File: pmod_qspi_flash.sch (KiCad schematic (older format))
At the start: 1 part, among them P1 PMOD-Device-x2-Type-Generic-A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

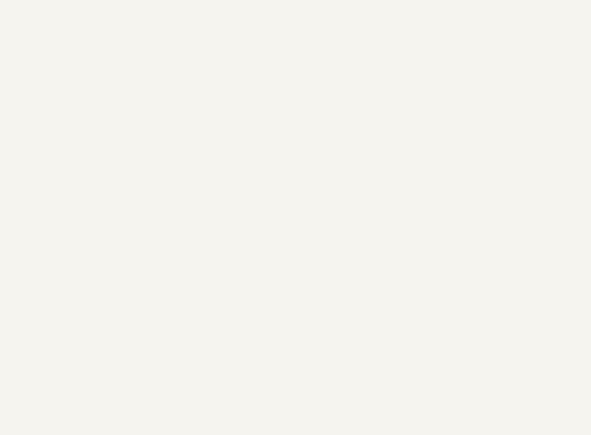
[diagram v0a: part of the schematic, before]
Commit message: add qspi flash symbol and footprint
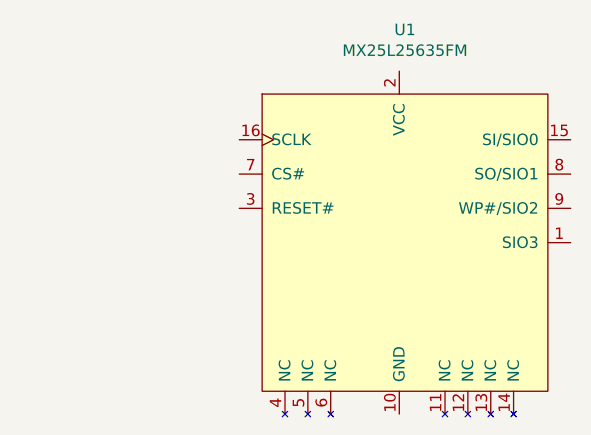
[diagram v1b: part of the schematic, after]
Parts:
- added U1: MX25L25635FM, Package_SO:SOIC-16W_7.5x10.3mm_P1.27mm, symbol qspi_flash:MX25L25635FM
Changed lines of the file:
@@
+	1    0    0    -1
+$EndComp
+$Comp
+L qspi_flash:MX25L25635FM U1
+U 1 1 6135200C
+P 5550 3750
+F 0 "U1" H 5575 4681 50  0000 C CNN
+F 1 "MX25L25635FM" H 5575 4590 50  0000 C CNN
+F 2 "Package_SO:SOIC-16W_7.5x10.3mm_P1.27mm" H 5050 4500 50  0001 C CNN
+F 3 "" H 5050 4500 50  0001 C CNN
+	1    5550 3750
 	1    0    0    -1
 $EndComp

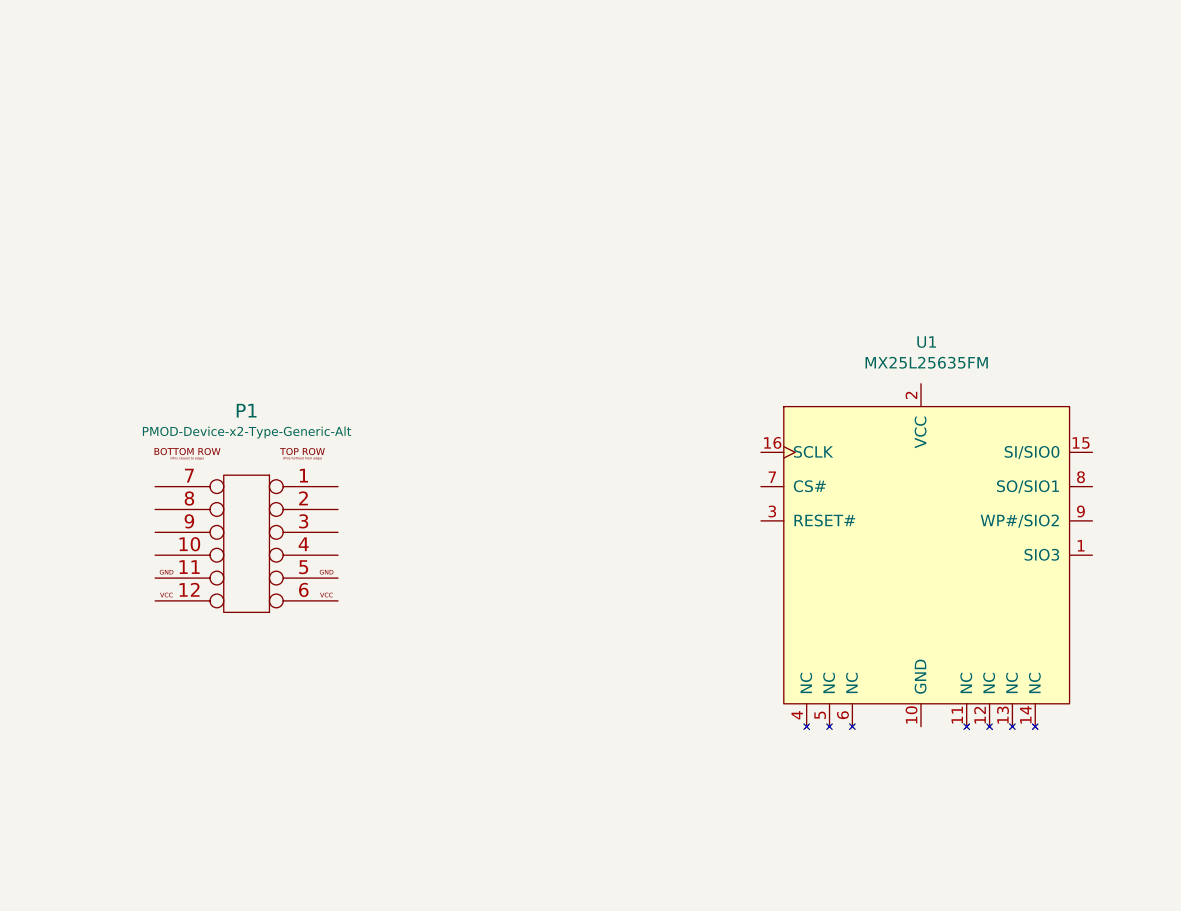
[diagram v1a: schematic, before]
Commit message: routed but ugly, need to rotate flash to align with signals
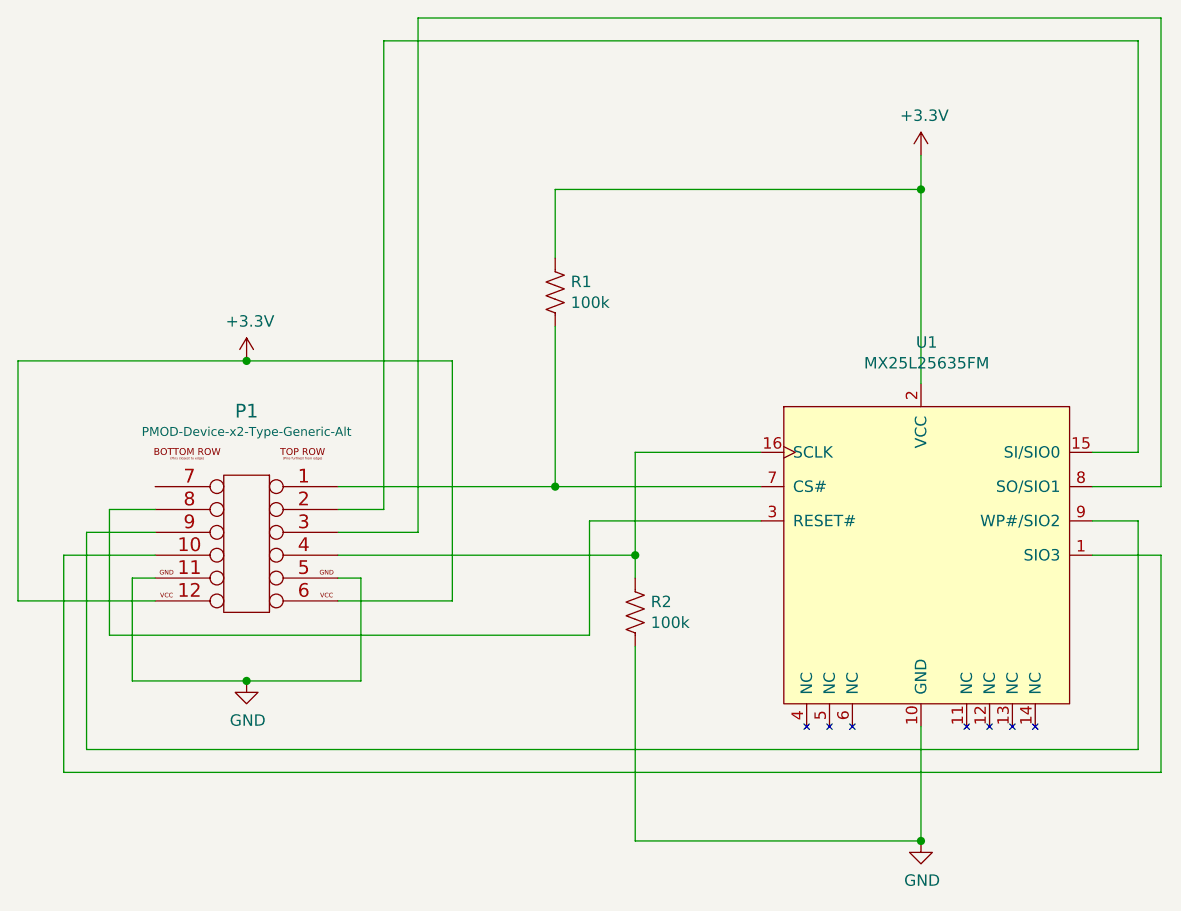
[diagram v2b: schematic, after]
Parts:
- added R1, R2: 100k, Resistor_SMD:R_1206_3216Metric_Pad1.30x1.75mm_HandSolder, symbol Device:R_US
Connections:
- net at P1.1 (P1): now also U1.7 (CS#), R1.2
- net at P1.10 (P10): now also U1.1 (SIO3)
- net GND: now reaches P1.11 (P11)
- net GND: now also P1.5 (P5), U1.10 (GND), R2.2
- net +3V3: now reaches P1.12 (P12)
- net +3V3: now also P1.6 (P6), U1.2 (VCC), R1.1
- net at P1.2 (P2): now also U1.15 (SI/SIO0)
- net at P1.3 (P3): now also U1.8 (SO/SIO1)
- net at P1.4 (P4): now also U1.16 (SCLK), R2.1
- net at P1.8 (P8): now also U1.3 (RESET#)
- net at P1.9 (P9): now also U1.9 (WP#/SIO2)
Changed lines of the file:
@@
 	1    0    0    -1
 $EndComp
+$Comp
+L Device:R_US R2
+U 1 1 6135558D
+P 4300 4000
+F 0 "R2" H 4368 4046 50  0000 L CNN
+F 1 "100k" H 4368 3955 50  0000 L CNN
+F 2 "Resistor_SMD:R_1206_3216Metric_Pad1.30x1.75mm_HandSolder" V 4340 3990 50  0001 C CNN
+F 3 "~" H 4300 4000 50  0001 C CNN
+	1    4300 4000
+	1    0    0    -1
+$EndComp
+$Comp
+L Device:R_US R1
+U 1 1 61358494
+P 3950 2600
+F 0 "R1" H 4018 2646 50  0000 L CNN
+F 1 "100k" H 4018 2555 50  0000 L CNN
+F 2 "Resistor_SMD:R_1206_3216Metric_Pad1.30x1.75mm_HandSolder" V 3990 2590 50  0001 C CNN
+F 3 "~" H 3950 2600 50  0001 C CNN
+	1    3950 2600
+	1    0    0    -1
+$EndComp
+Wire Wire Line
+	3950 2750 3950 3450
+Wire Wire Line
+	3950 3450 4850 3450
+Wire Wire Line
+	4850 3300 4300 3300
+Wire Wire Line
+	4300 3300 4300 3750
+$Comp
+L power:GND #PWR?
+U 1 1 6135AB99
+P 5550 5000
+F 0 "#PWR?" H 5550 4750 50  0001 C CNN
+F 1 "GND" H 5555 4827 50  0000 C CNN
+F 2 "" H 5550 5000 50  0001 C CNN
+F 3 "" H 5550 5000 50  0001 C CNN
+	1    5550 5000
+	1    0    0    -1
+$EndComp
+Wire Wire Line
+	5550 4500 5550 5000
+Wire Wire Line
+	5550 5000 4300 5000
+Wire Wire Line
+	4300 5000 4300 4150
+Connection ~ 5550 5000
+$Comp
+L power:+3.3V #PWR?
+U 1 1 6135B916
+P 5550 2000
+F 0 "#PWR?" H 5550 1850 50  0001 C CNN
+F 1 "+3.3V" H 5565 2173 50  0000 C CNN
+F 2 "" H 5550 2000 50  0001 C CNN
+F 3 "" H 5550 2000 50  0001 C CNN
+	1    5550 2000
+	1    0    0    -1
+$EndComp
+$Comp
+L power:+3.3V #PWR?
+U 1 1 6135C0DE
+P 2600 2900
+F 0 "#PWR?" H 2600 2750 50  0001 C CNN
+F 1 "+3.3V" H 2615 3073 50  0000 C CNN
+F 2 "" H 2600 2900 50  0001 C CNN
+F 3 "" H 2600 2900 50  0001 C CNN
+	1    2600 2900
+	1    0    0    -1
+$EndComp
+$Comp
+L power:GND #PWR?
+U 1 1 6135C78B
+P 2600 4300
+F 0 "#PWR?" H 2600 4050 50  0001 C CNN
+F 1 "GND" H 2605 4127 50  0000 C CNN
+F 2 "" H 2600 4300 50  0001 C CNN
+F 3 "" H 2600 4300 50  0001 C CNN
+	1    2600 4300
+	1    0    0    -1
+$EndComp
+Wire Wire Line
+	5550 2000 5550 2150
+Wire Wire Line
+	3950 2450 3950 2150
+Wire Wire Line
+	3950 2150 5550 2150
+Connection ~ 5550 2150
+Wire Wire Line
+	5550 2150 5550 3000
+Wire Wire Line
+	3950 3450 3000 3450
+Connection ~ 3950 3450
+Wire Wire Line
+	3000 3550 3200 3550
+Wire Wire Line
+	3200 3550 3200 1500
+Wire Wire Line
+	3200 1500 6500 1500
+Wire Wire Line
+	6500 1500 6500 3300
+Wire Wire Line
+	6500 3300 6300 3300
+Wire Wire Line
+	3000 3650 3350 3650
+Wire Wire Line
+	3350 3650 3350 1400
+Wire Wire Line
+	3350 1400 6600 1400
+Wire Wire Line
+	6600 1400 6600 3450
+Wire Wire Line
+	6600 3450 6300 3450
+Wire Wire Line
+	3000 3750 4300 3750
+Connection ~ 4300 3750
+Wire Wire Line
+	4300 3750 4300 3850
+Wire Wire Line
+	2200 3550 2000 3550
+Wire Wire Line
+	2000 3550 2000 4100
+Wire Wire Line
+	2000 4100 4100 4100
+Wire Wire Line
+	4100 4100 4100 3600
+Wire Wire Line
+	4100 3600 4850 3600
+Wire Wire Line
+	6300 3600 6500 3600
+Wire Wire Line
+	6500 3600 6500 4600
+Wire Wire Line
+	6500 4600 1900 4600
+Wire Wire Line
+	1900 4600 1900 3650
+Wire Wire Line
+	1900 3650 2200 3650
+Wire Wire Line
+	2200 3750 1800 3750
+Wire Wire Line
+	1800 3750 1800 4700
+Wire Wire Line
+	1800 4700 6600 4700
+Wire Wire Line
+	6600 4700 6600 3750
+Wire Wire Line
+	6600 3750 6300 3750
+Wire Wire Line
+	3000 3850 3100 3850
+Wire Wire Line
+	3100 3850 3100 4300
+Wire Wire Line
+	3100 4300 2600 4300
+Wire Wire Line
+	2600 4300 2100 4300
+Wire Wire Line
+	2100 4300 2100 3850
+Wire Wire Line
+	2100 3850 2200 3850
+Connection ~ 2600 4300
+Wire Wire Line
+	2200 3950 1600 3950
+Wire Wire Line
+	1600 3950 1600 2900
+Wire Wire Line
+	1600 2900 2600 2900
+Wire Wire Line
+	3500 2900 3500 3950
+Wire Wire Line
+	3500 3950 3000 3950
+Connection ~ 2600 2900
+Wire Wire Line
+	2600 2900 3500 2900
 $EndSCHEMATC

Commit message: rotate qspi flash, shorter traces
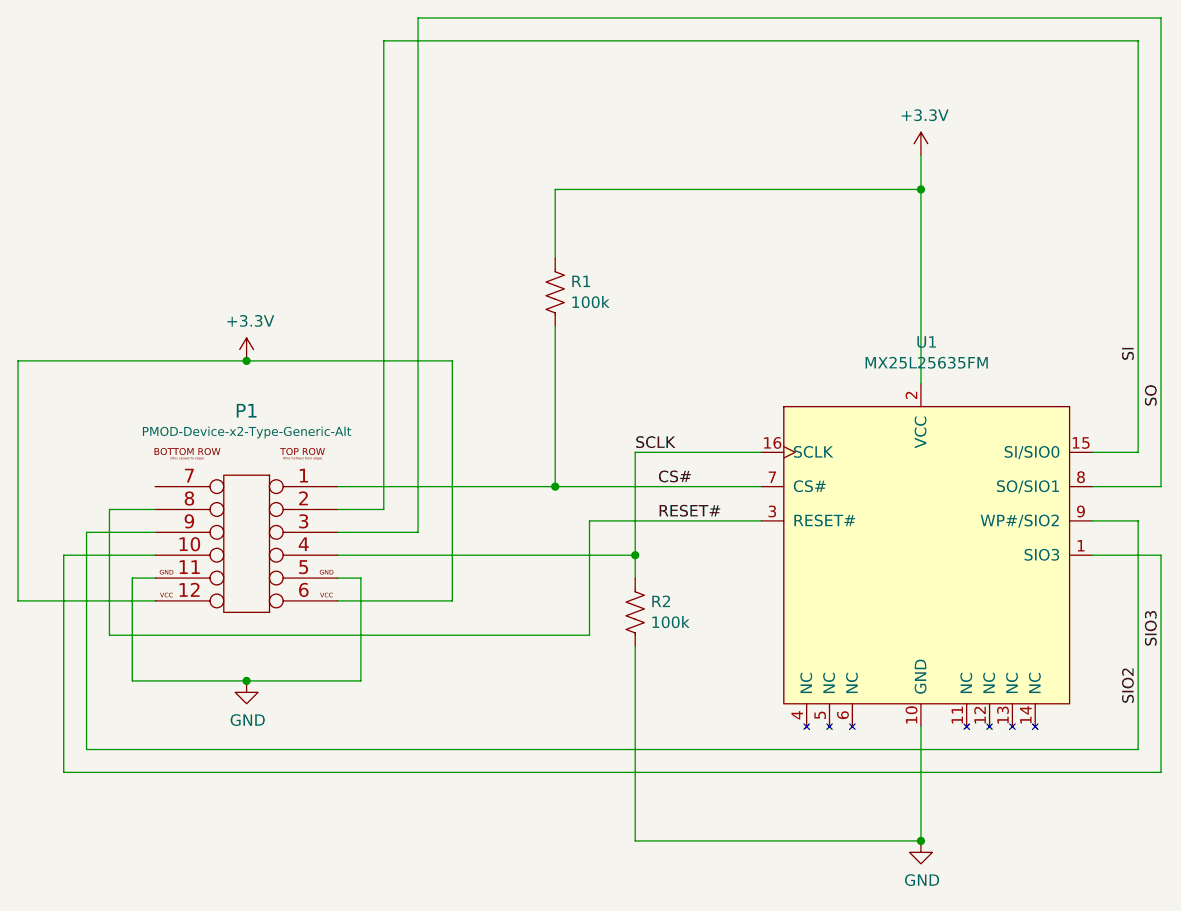
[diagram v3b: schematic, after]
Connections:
- net CS#: now reaches P1.1 (P1), R1.2, U1.7 (CS#)
- net SIO3: now reaches P1.10 (P10), U1.1 (SIO3)
- net SI: now reaches P1.2 (P2), U1.15 (SI/SIO0)
- net SO: now reaches P1.3 (P3), U1.8 (SO/SIO1)
- net SCLK: now reaches P1.4 (P4), R2.1, U1.16 (SCLK)
- net RESET#: now reaches P1.8 (P8), U1.3 (RESET#)
- net SIO2: now reaches P1.9 (P9), U1.9 (WP#/SIO2)
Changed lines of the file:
@@
 	4300 3300 4300 3750
 $Comp
-L power:GND #PWR?
+L power:GND #PWR04
 U 1 1 6135AB99
 P 5550 5000
-F 0 "#PWR?" H 5550 4750 50  0001 C CNN
+F 0 "#PWR04" H 5550 4750 50  0001 C CNN
 F 1 "GND" H 5555 4827 50  0000 C CNN
 F 2 "" H 5550 5000 50  0001 C CNN
@@
 Connection ~ 5550 5000
 $Comp
-L power:+3.3V #PWR?
+L power:+3.3V #PWR03
 U 1 1 6135B916
 P 5550 2000
-F 0 "#PWR?" H 5550 1850 50  0001 C CNN
+F 0 "#PWR03" H 5550 1850 50  0001 C CNN
 F 1 "+3.3V" H 5565 2173 50  0000 C CNN
 F 2 "" H 5550 2000 50  0001 C CNN
@@
 $EndComp
 $Comp
-L power:+3.3V #PWR?
+L power:+3.3V #PWR01
 U 1 1 6135C0DE
 P 2600 2900
-F 0 "#PWR?" H 2600 2750 50  0001 C CNN
+F 0 "#PWR01" H 2600 2750 50  0001 C CNN
 F 1 "+3.3V" H 2615 3073 50  0000 C CNN
 F 2 "" H 2600 2900 50  0001 C CNN
@@
 $EndComp
 $Comp
-L power:GND #PWR?
+L power:GND #PWR02
 U 1 1 6135C78B
 P 2600 4300
-F 0 "#PWR?" H 2600 4050 50  0001 C CNN
+F 0 "#PWR02" H 2600 4050 50  0001 C CNN
 F 1 "GND" H 2605 4127 50  0000 C CNN
 F 2 "" H 2600 4300 50  0001 C CNN
@@
 	1800 4700 6600 4700
 Wire Wire Line
-	6600 4700 6600 3750
-Wire Wire Line
 	6600 3750 6300 3750
 Wire Wire Line
@@
 Wire Wire Line
 	2600 2900 3500 2900
+Text Label 4300 3300 0    50   ~ 0
+SCLK
+Text Label 4400 3450 0    50   ~ 0
+CS#
+Text Label 4400 3600 0    50   ~ 0
+RESET#
+Text Label 6600 4150 1    50   ~ 0
+SIO3
+Wire Wire Line
+	6600 4700 6600 3750
+Text Label 6500 4400 1    50   ~ 0
+SIO2
+Text Label 6500 2900 1    50   ~ 0
+SI
+Text Label 6600 3100 1    50   ~ 0
+SO
 $EndSCHEMATC
